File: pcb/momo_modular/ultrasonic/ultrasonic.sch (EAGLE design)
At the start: 34 parts, among them U1 TDC1000, U2 TDC7200, U3 PIC16LF1847

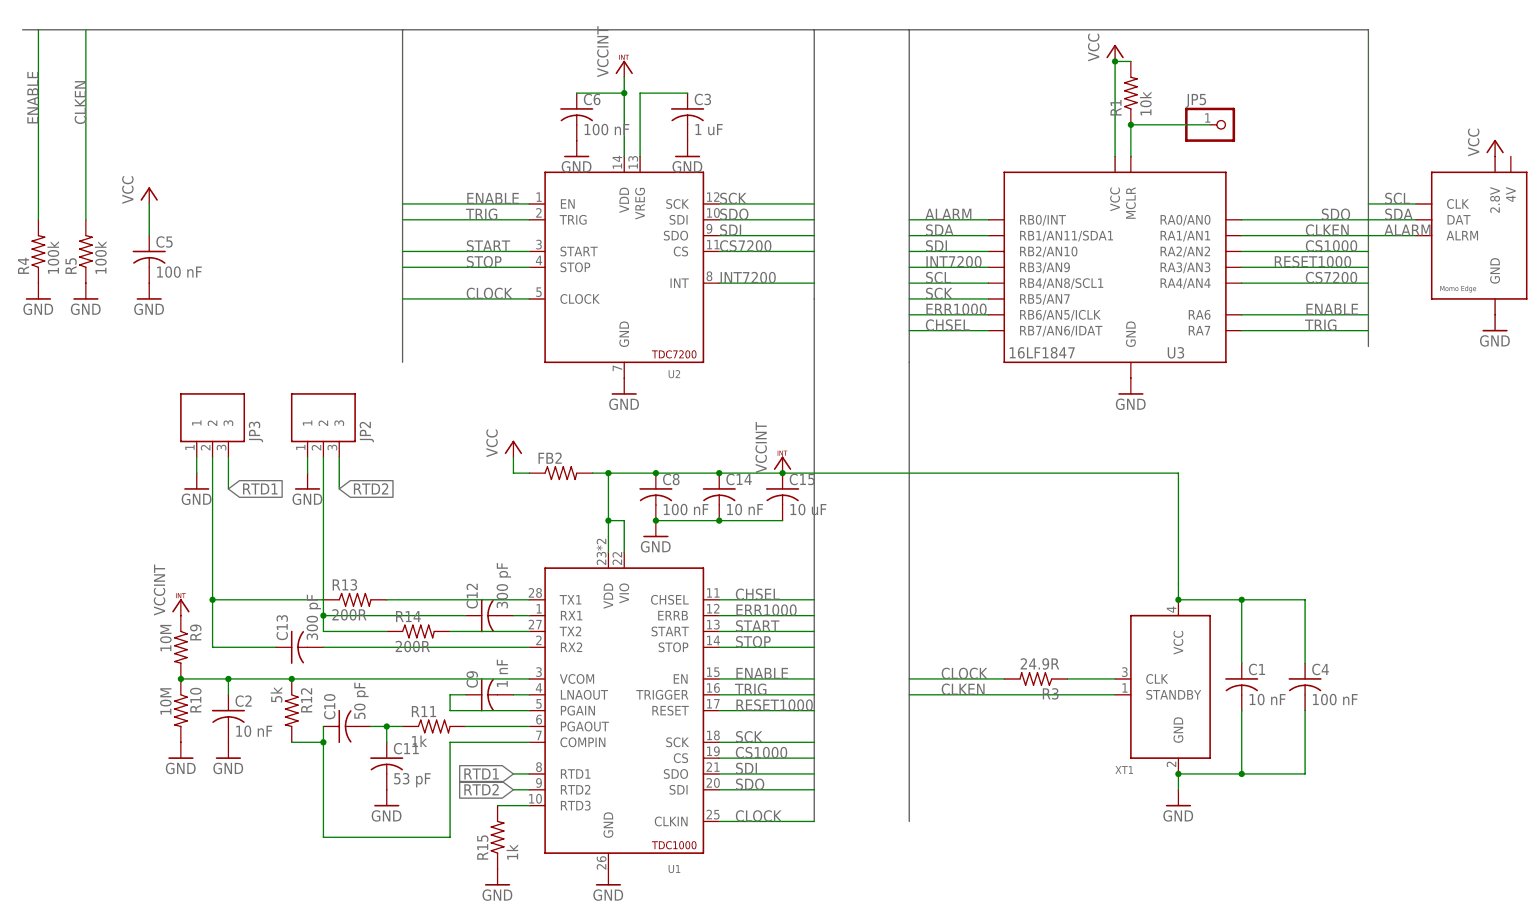
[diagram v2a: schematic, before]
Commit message: Finish laying out ultrasonic dev board
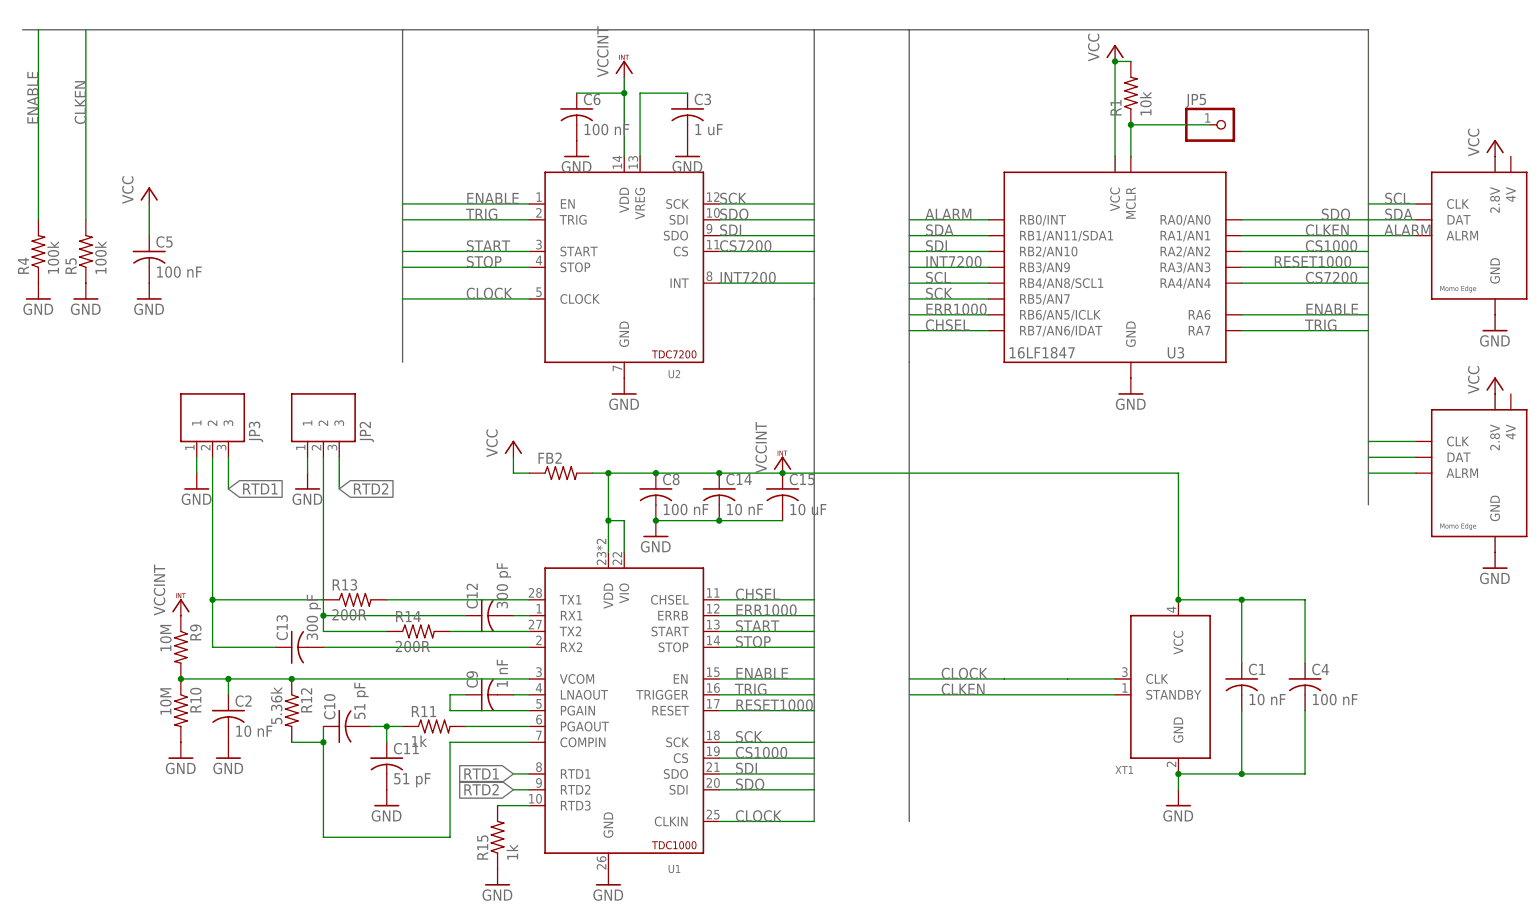
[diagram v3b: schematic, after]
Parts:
- removed R3: 24.9R, rcl:R-US_R0402
- added JP4: MOMO-EDGE-6M-RIGHT, components:MOMO-EDGE-6M-RIGHT
- C1, C14, C2: DIGIKEY-PN (none) -> 490-4516-1-ND
- C10: value 50 pF -> 51 pF; DIGIKEY-PN (none) -> 490-5944-1-ND
- C11: value 53 pF -> 51 pF; DIGIKEY-PN (none) -> 490-5944-1-ND
- C12, C13: DIGIKEY-PN (none) -> 490-3234-1-ND
- C15: DIGIKEY-PN (none) -> 490-10516-1-ND
- C3: DIGIKEY-PN (none) -> 490-3890-1-ND
- C4, C5, C6, C8: DIGIKEY-PN (none) -> 490-1318-1-ND
- C9: DIGIKEY-PN (none) -> 490-6349-1-ND
- R1: DIGIKEY-PN (none) -> RHM10.0KCDCT-ND
- R10, R9: DIGIKEY-PN (none) -> 1276-3434-1-ND
- R11: DIGIKEY-PN (none) -> RHM1.00KCDCT-ND
- R12: value 5k -> 5.36k; DIGIKEY-PN (none) -> RHM5.36KCDCT-ND
- R13, R14: DIGIKEY-PN (none) -> 311-200LRCT-ND
- R15: DIGIKEY-PN (none) -> P1.0KDCCT-ND
- R4, R5: DIGIKEY-PN (none) -> RHM100KCDCT-ND
- U1: MPN (none) -> TDC1000PW
- U2: MPN (none) -> TDC7200PW
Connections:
- removed net N$3: R3.1, XT1.CLK
- net ALARM: now also JP4.ALRM
- net CLOCK: now also XT1.CLK; no longer R3.2
- net GND: now also JP4.GND
- net SCL: now also JP4.CLK
- net SDA: now also JP4.DAT
- net VCC: now also JP4.2.8V
